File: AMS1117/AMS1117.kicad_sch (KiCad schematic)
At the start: 0 parts

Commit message: added global label
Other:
- sheet LDO_3V3_AMS1117 renamed LDO_3V3_AMS1117_
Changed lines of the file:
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@@
 	(generator_version "8.0")
 	(paper "A4")
+	(wire
+		(pts
+			(xy 63.5 41.91) (xy 60.96 41.91)
+		)
+		(stroke
+			(width 0)
+			(type default)
+		)
+	)
+	(global_label "3v3"
+		(shape input)
+		(at 63.5 41.91 0)
+		(fields_autoplaced yes)
+		(effects
+			(font
+				(size 1.27 1.27)
+			)
+			(justify left)
+		)
+		(property "Intersheetrefs" "${INTERSHEET_REFS}"
+			(at 69.8718 41.91 0)
+			(effects
+				(font
+					(size 1.27 1.27)
+				)
+				(justify left)
+				(hide yes)
+			)
+		)
+	)
 	(sheet
-		(at 19.05 15.24)
+		(at 46.99 38.1)
 		(size 13.97 7.62)
 		(stroke
@@
 			(color 0 0 0 0.0000)
 		)
-		(property "Sheetname" "LDO_3V3_AMS1117"
-			(at 16.51 14.732 0)
+		(property "Sheetname" "LDO_3V3_AMS1117_"
+			(at 44.45 37.592 0)
 			(effects
 				(font
@@
 		)
 		(property "Sheetfile" "LDO_3V3_AMS1117.kicad_sch"
-			(at 12.192 23.622 0)
+			(at 40.132 46.482 0)
 			(effects
 				(font
@@
 		)
 		(pin "3V3" output
-			(at 33.02 19.05 0)
+			(at 60.96 41.91 0)
 			(effects
 				(font
@@
 		)
 		(pin "VCC" input
-			(at 19.05 19.05 180)
+			(at 46.99 41.91 180)
 			(effects
 				(font

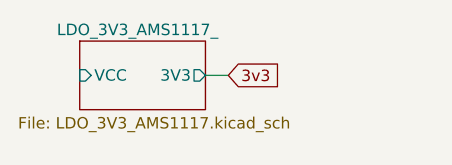
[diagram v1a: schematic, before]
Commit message: added '?' to the sheet designator to be replaced while coling
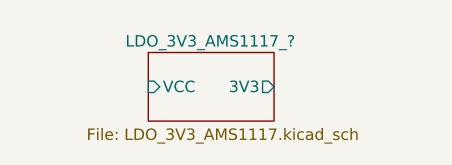
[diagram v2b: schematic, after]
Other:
- sheet LDO_3V3_AMS1117_ renamed LDO_3V3_AMS1117_?
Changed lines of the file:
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@@
 	(generator_version "8.0")
 	(paper "A4")
-	(wire
-		(pts
-			(xy 63.5 41.91) (xy 60.96 41.91)
-		)
-		(stroke
-			(width 0)
-			(type default)
-		)
-	)
-	(global_label "3v3"
-		(shape input)
-		(at 63.5 41.91 0)
-		(fields_autoplaced yes)
-		(effects
-			(font
-				(size 1.27 1.27)
-			)
-			(justify left)
-		)
-		(property "Intersheetrefs" "${INTERSHEET_REFS}"
-			(at 69.8718 41.91 0)
-			(effects
-				(font
-					(size 1.27 1.27)
-				)
-				(justify left)
-				(hide yes)
-			)
-		)
-	)
 	(sheet
-		(at 46.99 38.1)
+		(at 54.61 39.37)
 		(size 13.97 7.62)
 		(stroke
@@
 			(color 0 0 0 0.0000)
 		)
-		(property "Sheetname" "LDO_3V3_AMS1117_"
-			(at 44.45 37.592 0)
+		(property "Sheetname" "LDO_3V3_AMS1117_?"
+			(at 52.07 38.862 0)
 			(effects
 				(font
@@
 		)
 		(property "Sheetfile" "LDO_3V3_AMS1117.kicad_sch"
-			(at 40.132 46.482 0)
+			(at 47.752 47.752 0)
 			(effects
 				(font
@@
 		)
 		(pin "3V3" output
-			(at 60.96 41.91 0)
+			(at 68.58 43.18 0)
 			(effects
 				(font
@@
 		)
 		(pin "VCC" input
-			(at 46.99 41.91 180)
+			(at 54.61 43.18 180)
 			(effects
 				(font

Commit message: added gnd
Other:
- sheet LDO_3V3_AMS1117_? ports: added GND; removed none
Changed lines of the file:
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@@
 		)
 		(pin "3V3" output
-			(at 68.58 43.18 0)
+			(at 68.58 41.91 0)
 			(effects
 				(font
@@
 		)
 		(pin "VCC" input
-			(at 54.61 43.18 180)
+			(at 54.61 41.91 180)
 			(effects
 				(font
@@
 			)
 		)
+		(pin "GND" bidirectional
+			(at 68.58 44.45 0)
+			(effects
+				(font
+					(size 1.27 1.27)
+				)
+				(justify right)
+			)
+		)

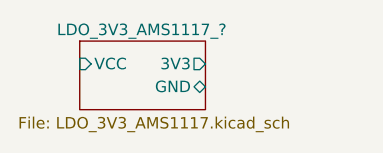
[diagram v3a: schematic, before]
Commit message: changes in, out for ams1117
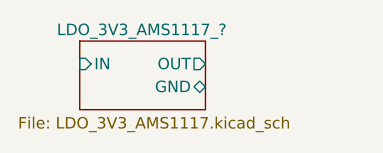
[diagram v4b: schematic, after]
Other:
- sheet LDO_3V3_AMS1117_? ports: added IN, OUT; removed 3V3, VCC
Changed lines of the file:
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@@
-			)
-		)
-		(pin "3V3" output
-			(at 68.58 41.91 0)
-			(effects
-				(font
-					(size 1.27 1.27)
-				)
-				(justify right)
-			)
-		)
-		(pin "VCC" input
-			(at 54.61 41.91 180)
-			(effects
-				(font
-					(size 1.27 1.27)
-				)
-				(justify left)
 			)
 		)
@@
 			)
 		)
+		(pin "OUT" output
+			(at 68.58 41.91 0)
+			(effects
+				(font
+					(size 1.27 1.27)
+				)
+				(justify right)
+			)
+		)
+		(pin "IN" input
+			(at 54.61 41.91 180)
+			(effects
+				(font
+					(size 1.27 1.27)
+				)
+				(justify left)
+			)
+		)
